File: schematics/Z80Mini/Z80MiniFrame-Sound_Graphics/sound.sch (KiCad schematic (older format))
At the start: 17 parts, among them U7 AY-3-8910, U8 74LS02, U9 LM386, X1 ACO-2MHz

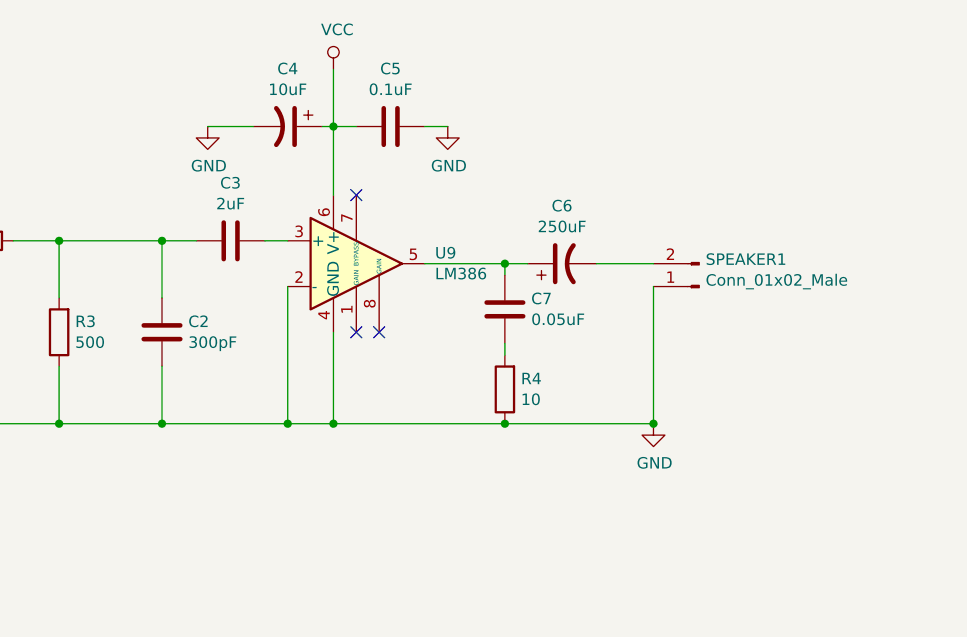
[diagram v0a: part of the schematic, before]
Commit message: Latest graphics and sound card schematic and PCB modifications
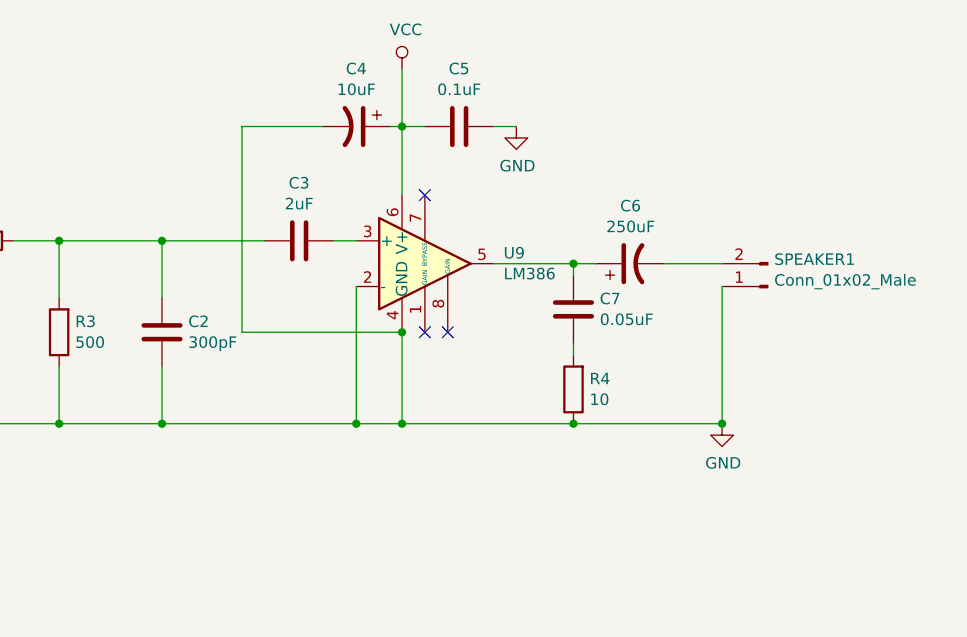
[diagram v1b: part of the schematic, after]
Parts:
- C4: footprint (none) -> Capacitor_THT:CP_Radial_D5.0mm_P2.00mm
- C5: footprint (none) -> Capacitor_THT:C_Disc_D7.0mm_W2.5mm_P5.00mm
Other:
- moved on the sheet: C3, C4, C5, C6, C7, R4, SPEAKER1, U9
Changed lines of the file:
@@
 L power:GND #PWR?
 U 1 1 5D7989A4
-P 9300 3050
+P 9600 3050
 AR Path="/5D7989A4" Ref="#PWR?"  Part="1"
 AR Path="/5D76ACBB/5D7989A4" Ref="#PWR0109"  Part="1"
-F 0 "#PWR0109" H 9300 2800 50  0001 C CNN
-F 1 "GND" H 9305 2877 50  0000 C CNN
-F 2 "" H 9300 3050 50  0001 C CNN
-F 3 "" H 9300 3050 50  0001 C CNN
-	1    9300 3050
+F 0 "#PWR0109" H 9600 2800 50  0001 C CNN
+F 1 "GND" H 9605 2877 50  0000 C CNN
+F 2 "" H 9600 3050 50  0001 C CNN
+F 3 "" H 9600 3050 50  0001 C CNN
+	1    9600 3050
 	1    0    0    -1
 $EndComp
@@
 L Device:C C?
 U 1 1 5D7989B0
-P 7450 2250
+P 7750 2250
 AR Path="/5D7989B0" Ref="C?"  Part="1"
 AR Path="/5D76ACBB/5D7989B0" Ref="C3"  Part="1"
-F 0 "C3" V 7198 2250 50  0000 C CNN
-F 1 "2uF" V 7289 2250 50  0000 C CNN
-F 2 "Capacitor_THT:C_Disc_D5.0mm_W2.5mm_P5.00mm" H 7488 2100 50  0001 C CNN
-F 3 "~" H 7450 2250 50  0001 C CNN
-	1    7450 2250
+F 0 "C3" V 7498 2250 50  0000 C CNN
+F 1 "2uF" V 7589 2250 50  0000 C CNN
+F 2 "Capacitor_THT:C_Disc_D5.0mm_W2.5mm_P5.00mm" H 7788 2100 50  0001 C CNN
+F 3 "~" H 7750 2250 50  0001 C CNN
+	1    7750 2250
 	0    1    1    0
 $EndComp
 Wire Wire Line
-	7600 2250 7700 2250
+	7900 2250 8000 2250
 Wire Wire Line
 	6700 3050 6000 3050
@@
 L Amplifier_Audio:LM386 U?
 U 1 1 5D7989C3
-P 8000 2350
+P 8300 2350
 AR Path="/5D7989C3" Ref="U?"  Part="1"
 AR Path="/5D76ACBB/5D7989C3" Ref="U9"  Part="1"
-F 0 "U9" H 8344 2396 50  0000 L CNN
-F 1 "LM386" H 8344 2305 50  0000 L CNN
-F 2 "Package_DIP:DIP-8_W7.62mm_LongPads" H 8100 2450 50  0001 C CNN
-F 3 "http://www.ti.com/lit/ds/symlink/lm386.pdf" H 8200 2550 50  0001 C CNN
-	1    8000 2350
+F 0 "U9" H 8644 2396 50  0000 L CNN
+F 1 "LM386" H 8644 2305 50  0000 L CNN
+F 2 "Package_DIP:DIP-8_W7.62mm_LongPads" H 8400 2450 50  0001 C CNN
+F 3 "http://www.ti.com/lit/ds/symlink/lm386.pdf" H 8500 2550 50  0001 C CNN
+	1    8300 2350
 	1    0    0    -1
 $EndComp
@@
 L power:VCC #PWR?
 U 1 1 5D7989CB
-P 7900 1500
+P 8200 1500
 AR Path="/5D7989CB" Ref="#PWR?"  Part="1"
 AR Path="/5D76ACBB/5D7989CB" Ref="#PWR0110"  Part="1"
-F 0 "#PWR0110" H 7900 1350 50  0001 C CNN
-F 1 "VCC" H 7917 1673 50  0000 C CNN
-F 2 "" H 7900 1500 50  0001 C CNN
-F 3 "" H 7900 1500 50  0001 C CNN
-	1    7900 1500
-	1    0    0    -1
-$EndComp
-Wire Wire Line
-	7900 3050 7700 3050
-Connection ~ 7700 3050
-Wire Wire Line
-	7900 1500 7900 1750
-Wire Wire Line
-	8300 2350 8650 2350
+F 0 "#PWR0110" H 8200 1350 50  0001 C CNN
+F 1 "VCC" H 8217 1673 50  0000 C CNN
+F 2 "" H 8200 1500 50  0001 C CNN
+F 3 "" H 8200 1500 50  0001 C CNN
+	1    8200 1500
+	1    0    0    -1
+$EndComp
+Wire Wire Line
+	8200 3050 8000 3050
+Connection ~ 8000 3050
+Wire Wire Line
+	8200 1500 8200 1750
+Wire Wire Line
+	8600 2350 8950 2350
 $Comp
 L Device:CP1 C?
 U 1 1 5D7989D6
-P 8900 2350
+P 9200 2350
 AR Path="/5D7989D6" Ref="C?"  Part="1"
 AR Path="/5D76ACBB/5D7989D6" Ref="C6"  Part="1"
-F 0 "C6" V 9152 2350 50  0000 C CNN
-F 1 "250uF" V 9061 2350 50  0000 C CNN
-F 2 "Capacitor_THT:CP_Radial_D6.3mm_P2.50mm" H 8900 2350 50  0001 C CNN
-F 3 "~" H 8900 2350 50  0001 C CNN
-	1    8900 2350
+F 0 "C6" V 9452 2350 50  0000 C CNN
+F 1 "250uF" V 9361 2350 50  0000 C CNN
+F 2 "Capacitor_THT:CP_Radial_D6.3mm_P2.50mm" H 9200 2350 50  0001 C CNN
+F 3 "~" H 9200 2350 50  0001 C CNN
+	1    9200 2350
 	0    -1   -1   0
 $EndComp
 Wire Wire Line
-	9050 2350 9300 2350
+	9350 2350 9600 2350
 Connection ~ 5650 2850
-NoConn ~ 8000 2650
-NoConn ~ 8100 2650
-NoConn ~ 8000 2050
+NoConn ~ 8300 2650
+NoConn ~ 8400 2650
+NoConn ~ 8300 2050
 $Comp
 L Device:CP1 C?
 U 1 1 5D7989E4
-P 7700 1750
+P 8000 1750
 AR Path="/5D7989E4" Ref="C?"  Part="1"
 AR Path="/5D76ACBB/5D7989E4" Ref="C4"  Part="1"
-F 0 "C4" V 7448 1750 50  0000 C CNN
-F 1 "10uF" V 7539 1750 50  0000 C CNN
-F 2 "" H 7700 1750 50  0001 C CNN
-F 3 "~" H 7700 1750 50  0001 C CNN
-	1    7700 1750
+F 0 "C4" V 7748 1750 50  0000 C CNN
+F 1 "10uF" V 7839 1750 50  0000 C CNN
+F 2 "Capacitor_THT:CP_Radial_D5.0mm_P2.00mm" H 8000 1750 50  0001 C CNN
+F 3 "~" H 8000 1750 50  0001 C CNN
+	1    8000 1750
 	0    1    1    0
 $EndComp
 Wire Wire Line
-	7850 1750 7900 1750
-Connection ~ 7900 1750
-Wire Wire Line
-	7900 1750 7900 2050
-$Comp
-L power:GND #PWR?
-U 1 1 5D7989ED
-P 7350 1750
-AR Path="/5D7989ED" Ref="#PWR?"  Part="1"
-AR Path="/5D76ACBB/5D7989ED" Ref="#PWR0111"  Part="1"
-F 0 "#PWR0111" H 7350 1500 50  0001 C CNN
-F 1 "GND" H 7355 1577 50  0000 C CNN
-F 2 "" H 7350 1750 50  0001 C CNN
-F 3 "" H 7350 1750 50  0001 C CNN
-	1    7350 1750
-	1    0    0    -1
-$EndComp
-Wire Wire Line
-	7550 1750 7350 1750
+	8150 1750 8200 1750
+Connection ~ 8200 1750
+Wire Wire Line
+	8200 1750 8200 2050
 $Comp
 L Device:C C?
 U 1 1 5D7989F4
-P 8150 1750
+P 8450 1750
 AR Path="/5D7989F4" Ref="C?"  Part="1"
 AR Path="/5D76ACBB/5D7989F4" Ref="C5"  Part="1"
-F 0 "C5" V 8402 1750 50  0000 C CNN
-F 1 "0.1uF" V 8311 1750 50  0000 C CNN
-F 2 "" H 8188 1600 50  0001 C CNN
-F 3 "~" H 8150 1750 50  0001 C CNN
-	1    8150 1750
+F 0 "C5" V 8702 1750 50  0000 C CNN
+F 1 "0.1uF" V 8611 1750 50  0000 C CNN
+F 2 "Capacitor_THT:C_Disc_D7.0mm_W2.5mm_P5.00mm" H 8488 1600 50  0001 C CNN
+F 3 "~" H 8450 1750 50  0001 C CNN
+	1    8450 1750
 	0    -1   -1   0
 $EndComp
 Wire Wire Line
-	7900 1750 8000 1750
+	8200 1750 8300 1750
 $Comp
 L power:GND #PWR?
 U 1 1 5D7989FB
-P 8400 1750
+P 8700 1750
 AR Path="/5D7989FB" Ref="#PWR?"  Part="1"
 AR Path="/5D76ACBB/5D7989FB" Ref="#PWR0112"  Part="1"
-F 0 "#PWR0112" H 8400 1500 50  0001 C CNN
-F 1 "GND" H 8405 1577 50  0000 C CNN
-F 2 "" H 8400 1750 50  0001 C CNN
-F 3 "" H 8400 1750 50  0001 C CNN
-	1    8400 1750
-	1    0    0    -1
-$EndComp
-Wire Wire Line
-	8300 1750 8400 1750
+F 0 "#PWR0112" H 8700 1500 50  0001 C CNN
+F 1 "GND" H 8705 1577 50  0000 C CNN
+F 2 "" H 8700 1750 50  0001 C CNN
+F 3 "" H 8700 1750 50  0001 C CNN
+	1    8700 1750
+	1    0    0    -1
+$EndComp
+Wire Wire Line
+	8600 1750 8700 1750
 $Comp
 L Connector:Conn_01x02_Male SPEAKER?
 U 1 1 5D798A02
-P 9500 2450
+P 9800 2450
 AR Path="/5D798A02" Ref="SPEAKER?"  Part="1"
 AR Path="/5D76ACBB/5D798A02" Ref="SPEAKER1"  Part="1"
-F 0 "SPEAKER1" H 9472 2332 50  0000 R CNN
-F 1 "Conn_01x02_Male" H 9472 2423 50  0000 R CNN
-F 2 "Connector_Wire:SolderWirePad_1x02_P3.81mm_Drill1mm" H 9500 2450 50  0001 C CNN
-F 3 "~" H 9500 2450 50  0001 C CNN
-	1    9500 2450
+F 0 "SPEAKER1" H 9772 2332 50  0000 R CNN
+F 1 "Conn_01x02_Male" H 9772 2423 50  0000 R CNN
+F 2 "Connector_Wire:SolderWirePad_1x02_P3.81mm_Drill1mm" H 9800 2450 50  0001 C CNN
+F 3 "~" H 9800 2450 50  0001 C CNN
+	1    9800 2450
 	-1   0    0    1
 $EndComp
 Wire Wire Line
-	9300 3050 8650 3050
+	9600 3050 8950 3050
 Text HLabel 1850 2300 0    50   BiDi ~ 0
 D[0..7]
@@
 L Device:R R?
 U 1 1 5DB0E5F5
-P 8650 2900
+P 8950 2900
 AR Path="/5DB0E5F5" Ref="R?"  Part="1"
 AR Path="/5D76ACBB/5DB0E5F5" Ref="R4"  Part="1"
-F 0 "R4" H 8580 2854 50  0000 R CNN
-F 1 "10" H 8580 2945 50  0000 R CNN
-F 2 "Resistor_THT:R_Axial_DIN0207_L6.3mm_D2.5mm_P10.16mm_Horizontal" V 8580 2900 50  0001 C CNN
-F 3 "~" H 8650 2900 50  0001 C CNN
-	1    8650 2900
+F 0 "R4" H 8880 2854 50  0000 R CNN
+F 1 "10" H 8880 2945 50  0000 R CNN
+F 2 "Resistor_THT:R_Axial_DIN0207_L6.3mm_D2.5mm_P10.16mm_Horizontal" V 8880 2900 50  0001 C CNN
+F 3 "~" H 8950 2900 50  0001 C CNN
+	1    8950 2900
 	-1   0    0    1
 $EndComp
-Connection ~ 8650 3050
-Wire Wire Line
-	8650 3050 7900 3050
+Connection ~ 8950 3050
+Wire Wire Line
+	8950 3050 8200 3050
 $Comp
 L Device:C C?
 U 1 1 5DB1062D
-P 8650 2550
+P 8950 2550
 AR Path="/5DB1062D" Ref="C?"  Part="1"
 AR Path="/5D76ACBB/5DB1062D" Ref="C7"  Part="1"
-F 0 "C7" H 8765 2596 50  0000 L CNN
-F 1 "0.05uF" H 8765 2505 50  0000 L CNN
-F 2 "Capacitor_THT:C_Disc_D5.0mm_W2.5mm_P5.00mm" H 8688 2400 50  0001 C CNN
-F 3 "~" H 8650 2550 50  0001 C CNN
-	1    8650 2550
-	1    0    0    -1
-$EndComp
-Wire Wire Line
-	8650 2750 8650 2700
-Wire Wire Line
-	8650 2400 8650 2350
-Connection ~ 8650 2350
-Wire Wire Line
-	8650 2350 8750 2350
-Wire Wire Line
-	9300 2450 9300 3050
-Connection ~ 7900 3050
+F 0 "C7" H 9065 2596 50  0000 L CNN
+F 1 "0.05uF" H 9065 2505 50  0000 L CNN
+F 2 "Capacitor_THT:C_Disc_D5.0mm_W2.5mm_P5.00mm" H 8988 2400 50  0001 C CNN
+F 3 "~" H 8950 2550 50  0001 C CNN
+	1    8950 2550
+	1    0    0    -1
+$EndComp
+Wire Wire Line
+	8950 2750 8950 2700
+Wire Wire Line
+	8950 2400 8950 2350
+Connection ~ 8950 2350
+Wire Wire Line
+	8950 2350 9050 2350
+Wire Wire Line
+	9600 2450 9600 3050
+Connection ~ 8200 3050
 Wire Wire Line
 	5650 2250 6000 2250
@@
 	7150 2250 7150 2500
 Wire Wire Line
-	7700 2450 7700 3050
-Wire Wire Line
-	7900 2650 7900 3050
+	8000 2450 8000 3050
 Wire Wire Line
 	7150 2800 7150 3050
@@
 Wire Wire Line
 	5650 2250 5650 2850
-Connection ~ 9300 3050
-Connection ~ 7150 2250
-Wire Wire Line
-	7150 2250 7300 2250
-Connection ~ 7150 3050
-Wire Wire Line
-	7150 3050 7700 3050
+Connection ~ 9600 3050
 Wire Wire Line
 	6700 3050 7150 3050
@@
 Wire Wire Line
 	3850 6500 3850 6400
+Wire Wire Line
+	7150 3050 8000 3050
+Connection ~ 7150 3050
+Wire Wire Line
+	8200 2650 8200 3050
+Wire Wire Line
+	7850 1750 7500 1750
+Wire Wire Line
+	7500 1750 7500 2650
+Wire Wire Line
+	7500 2650 8200 2650
+Connection ~ 8200 2650
+Wire Wire Line
+	7600 2250 7150 2250
+Connection ~ 7150 2250
 Wire Bus Line
 	4200 2300 4200 3450

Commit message: Latest modifications on Graphics-Sound card
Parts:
- added J3: Conn_01x03_Male, Connector_PinHeader_2.00mm:PinHeader_1x03_P2.00mm_Vertical, symbol Connector:Conn_01x03_Male
- added JP1: PREAMP_MONO, Connector_PinHeader_2.00mm:PinHeader_2x03_P2.00mm_Vertical, symbol Connector_Generic:Conn_02x03_Odd_Even
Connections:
- new net: J3.2 (Pin_2), JP1.4 (Pin_4), U7.3 (ACH_B)
- new net: J3.1 (Pin_1), JP1.2 (Pin_2), U7.38 (ACH_C)
- new net: J3.3 (Pin_3), JP1.6 (Pin_6), U7.4 (ACH_A)
- new net: JP1.1 (Pin_1), JP1.3 (Pin_3), JP1.5 (Pin_5), R1.2, R2.2
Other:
- moved on the sheet: C1, C14, C2, C3, C4, C5, C6, C7, R1, R2, R3, R4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

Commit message: Latest modifications
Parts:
- added J4: IO_PORT, Connector_IDC:IDC-Header_2x08_P2.54mm_Vertical, symbol Connector_Generic:Conn_02x08_Odd_Even
- U7: symbol Audio:AY-3-8910 -> Z80MiniFrame-Sound_Graphics-rescue:AY-3-8910-Audio
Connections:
- net at U7.10 (IOB3): now also J4.8 (Pin_8)
- net at U7.11 (IOB2): now also J4.6 (Pin_6)
- net at U7.12 (IOB1): now also J4.4 (Pin_4)
- net at U7.13 (IOB0): now also J4.2 (Pin_2)
- net at U7.14 (IOA7): now also J4.15 (Pin_15)
- net at U7.15 (IOA6): now also J4.13 (Pin_13)
- net at U7.16 (IOA5): now also J4.11 (Pin_11)
- net at U7.17 (IOA4): now also J4.9 (Pin_9)
- net at U7.18 (IOA3): now also J4.7 (Pin_7)
- net at U7.19 (IOA2): now also J4.5 (Pin_5)
- net at U7.20 (IOA1): now also J4.3 (Pin_3)
- net at U7.21 (IOA0): now also J4.1 (Pin_1)
- net at U7.6 (IOB7): now also J4.16 (Pin_16)
- net at U7.7 (IOB6): now also J4.14 (Pin_14)
- net at U7.8 (IOB5): now also J4.12 (Pin_12)
- net at U7.9 (IOB4): now also J4.10 (Pin_10)
- no-connect marks 21 -> 5
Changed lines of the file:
@@
 Text HLabel 1550 3000 0    50   BiDi ~ 0
 D[0..7]
-NoConn ~ 5200 5550
-NoConn ~ 5200 5450
-NoConn ~ 5200 5350
-NoConn ~ 5200 5250
-NoConn ~ 5200 5150
-NoConn ~ 5200 5050
-NoConn ~ 5200 4950
-NoConn ~ 5200 4850
-NoConn ~ 5200 4650
-NoConn ~ 5200 4550
-NoConn ~ 5200 4450
-NoConn ~ 5200 4350
-NoConn ~ 5200 4250
-NoConn ~ 5200 4150
-NoConn ~ 5200 4050
-NoConn ~ 5200 3950
 Text HLabel 1700 4350 0    50   Input ~ 0
 A0
@@
 	8300 2650 7850 2650
 Connection ~ 7850 2650
-$Comp
-L Audio:AY-3-8910 U?
+Wire Wire Line
+	5200 3750 5450 3750
+Wire Wire Line
+	5200 3650 5350 3650
+Wire Wire Line
+	5200 3550 5250 3550
+Wire Wire Line
+	5250 3550 5250 3250
+Wire Wire Line
+	5350 3650 5350 3350
+Wire Wire Line
+	5450 3750 5450 3450
+$Comp
+L Connector_Generic:Conn_02x03_Odd_Even JP1
+U 1 1 5D7FB918
+P 6050 2850
+F 0 "JP1" V 6100 2650 50  0000 R CNN
+F 1 "PREAMP_MONO" H 6450 3100 50  0000 R CNN
+F 2 "Connector_PinHeader_2.00mm:PinHeader_2x03_P2.00mm_Vertical" H 6050 2850 50  0001 C CNN
+F 3 "~" H 6050 2850 50  0001 C CNN
+	1    6050 2850
+	0    1    1    0
+$EndComp
+Wire Wire Line
+	5450 3450 6150 3450
+Wire Wire Line
+	5350 3350 6050 3350
+Wire Wire Line
+	6700 2650 6700 2900
+Wire Wire Line
+	6050 3350 6050 3150
+Wire Wire Line
+	6150 3450 6150 3150
+Wire Wire Line
+	5250 3250 5950 3250
+Wire Wire Line
+	5950 3250 5950 3150
+Wire Wire Line
+	5950 2650 6050 2650
+Connection ~ 6050 2650
+Wire Wire Line
+	6050 2650 6150 2650
+Connection ~ 6150 2650
+Wire Wire Line
+	6150 2650 6700 2650
+Wire Wire Line
+	6700 2650 6900 2650
+Wire Wire Line
+	4450 3150 4450 2500
+Wire Wire Line
+	4400 2500 4450 2500
+Connection ~ 4450 2500
+Wire Wire Line
+	4450 2500 4450 2350
+Connection ~ 5250 3250
+Connection ~ 5350 3350
+Connection ~ 5450 3450
+$Comp
+L Connector:Conn_01x03_Male J3
+U 1 1 5D798F32
+P 5350 2400
+F 0 "J3" V 5412 2544 50  0000 L CNN
+F 1 "Conn_01x03_Male" V 5503 2544 50  0000 L CNN
+F 2 "Connector_PinHeader_2.00mm:PinHeader_1x03_P2.00mm_Vertical" H 5350 2400 50  0001 C CNN
+F 3 "~" H 5350 2400 50  0001 C CNN
+	1    5350 2400
+	0    1    1    0
+$EndComp
+Wire Wire Line
+	5250 2600 5250 3250
+Wire Wire Line
+	5350 2600 5350 3350
+Wire Wire Line
+	5450 2600 5450 3450
+$Comp
+L Z80MiniFrame-Sound_Graphics-rescue:AY-3-8910-Audio U?
 U 1 1 5D798962
 P 3400 3000
@@
 $EndComp
 Wire Wire Line
-	5200 3750 5450 3750
-Wire Wire Line
-	5200 3650 5350 3650
-Wire Wire Line
-	5200 3550 5250 3550
-Wire Wire Line
-	5250 3550 5250 3250
-Wire Wire Line
-	5350 3650 5350 3350
-Wire Wire Line
-	5450 3750 5450 3450
-$Comp
-L Connector_Generic:Conn_02x03_Odd_Even JP1
-U 1 1 5D7FB918
-P 6050 2850
-F 0 "JP1" V 6100 2650 50  0000 R CNN
-F 1 "PREAMP_MONO" H 6450 3100 50  0000 R CNN
-F 2 "Connector_PinHeader_2.00mm:PinHeader_2x03_P2.00mm_Vertical" H 6050 2850 50  0001 C CNN
-F 3 "~" H 6050 2850 50  0001 C CNN
-	1    6050 2850
-	0    1    1    0
-$EndComp
-Wire Wire Line
-	5450 3450 6150 3450
-Wire Wire Line
-	5350 3350 6050 3350
-Wire Wire Line
-	6700 2650 6700 2900
-Wire Wire Line
-	6050 3350 6050 3150
-Wire Wire Line
-	6150 3450 6150 3150
-Wire Wire Line
-	5250 3250 5950 3250
-Wire Wire Line
-	5950 3250 5950 3150
-Wire Wire Line
-	5950 2650 6050 2650
-Connection ~ 6050 2650
-Wire Wire Line
-	6050 2650 6150 2650
-Connection ~ 6150 2650
-Wire Wire Line
-	6150 2650 6700 2650
-Wire Wire Line
-	6700 2650 6900 2650
-Wire Wire Line
-	4450 3150 4450 2500
-Wire Wire Line
-	4400 2500 4450 2500
-Connection ~ 4450 2500
-Wire Wire Line
-	4450 2500 4450 2350
-Connection ~ 5250 3250
-Connection ~ 5350 3350
-Connection ~ 5450 3450
-$Comp
-L Connector:Conn_01x03_Male J3
-U 1 1 5D798F32
-P 5350 2400
-F 0 "J3" V 5412 2544 50  0000 L CNN
-F 1 "Conn_01x03_Male" V 5503 2544 50  0000 L CNN
-F 2 "Connector_PinHeader_2.00mm:PinHeader_1x03_P2.00mm_Vertical" H 5350 2400 50  0001 C CNN
-F 3 "~" H 5350 2400 50  0001 C CNN
-	1    5350 2400
-	0    1    1    0
-$EndComp
-Wire Wire Line
-	5250 2600 5250 3250
-Wire Wire Line
-	5350 2600 5350 3350
-Wire Wire Line
-	5450 2600 5450 3450
+	5200 3950 5600 3950
+Wire Wire Line
+	5200 4050 5600 4050
+Wire Wire Line
+	5600 4150 5200 4150
+Wire Wire Line
+	5200 4250 5600 4250
+Wire Wire Line
+	5200 4350 5600 4350
+Wire Wire Line
+	5200 4450 5600 4450
+Wire Wire Line
+	5600 4550 5200 4550
+Wire Wire Line
+	5200 4650 5600 4650
+Wire Wire Line
+	5200 4850 6200 4850
+Wire Wire Line
+	6200 4850 6200 3950
+Wire Wire Line
+	6200 3950 6100 3950
+Wire Wire Line
+	6300 4050 6100 4050
+Wire Wire Line
+	5200 4950 6300 4950
+Wire Wire Line
+	6300 4050 6300 4950
+Wire Wire Line
+	5200 5050 6400 5050
+Wire Wire Line
+	6400 5050 6400 4150
+Wire Wire Line
+	6400 4150 6100 4150
+Wire Wire Line
+	5200 5150 6500 5150
+Wire Wire Line
+	6500 5150 6500 4250
+Wire Wire Line
+	6500 4250 6100 4250
+Wire Wire Line
+	5200 5250 6600 5250
+Wire Wire Line
+	6600 5250 6600 4350
+Wire Wire Line
+	6600 4350 6100 4350
+Wire Wire Line
+	5200 5350 6700 5350
+Wire Wire Line
+	6700 5350 6700 4450
+Wire Wire Line
+	6700 4450 6100 4450
+Wire Wire Line
+	5200 5450 6800 5450
+Wire Wire Line
+	6800 5450 6800 4550
+Wire Wire Line
+	6800 4550 6100 4550
+$Comp
+L Connector_Generic:Conn_02x08_Odd_Even J4
+U 1 1 5D817986
+P 5800 4250
+F 0 "J4" H 5850 4767 50  0000 C CNN
+F 1 "IO_PORT" H 5850 4676 50  0000 C CNN
+F 2 "Connector_IDC:IDC-Header_2x08_P2.54mm_Vertical" H 5800 4250 50  0001 C CNN
+F 3 "~" H 5800 4250 50  0001 C CNN
+	1    5800 4250
+	1    0    0    -1
+$EndComp
+Wire Wire Line
+	5200 5550 6900 5550
+Wire Wire Line
+	6900 5550 6900 4650
+Wire Wire Line
+	6100 4650 6900 4650
 Wire Bus Line
 	3900 3000 3900 4150
